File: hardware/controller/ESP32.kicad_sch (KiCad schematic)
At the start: 41 parts, among them J3 Conn_01x05_Pin, Q3 SS8050-G, Q4 SS8050-G, U2 ESP32-S3, Y1 FH4000074Z

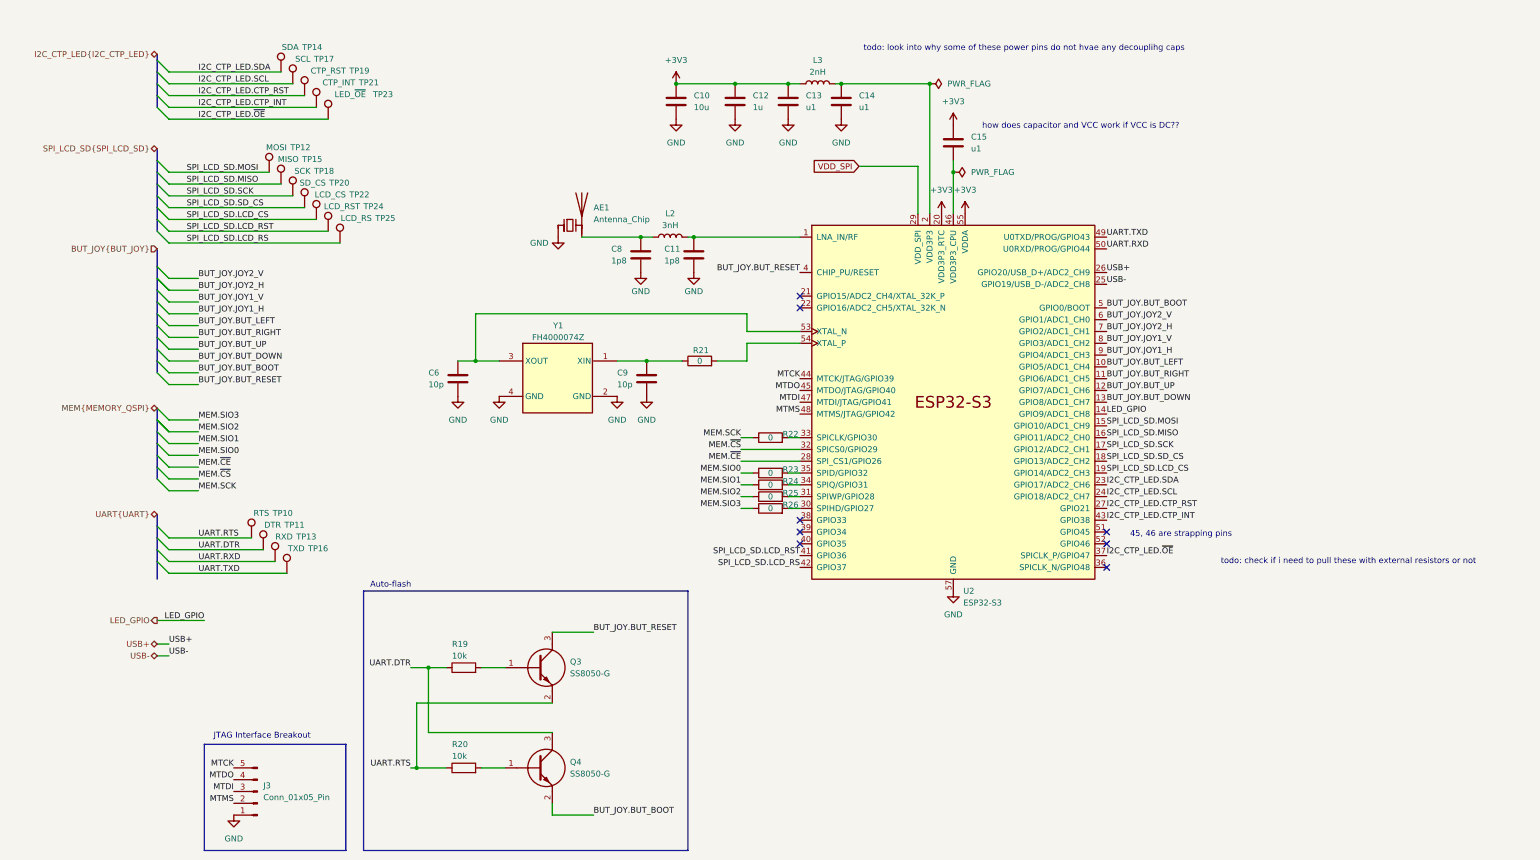
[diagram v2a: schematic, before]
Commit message: ERC good to go. grouped all components on pcb
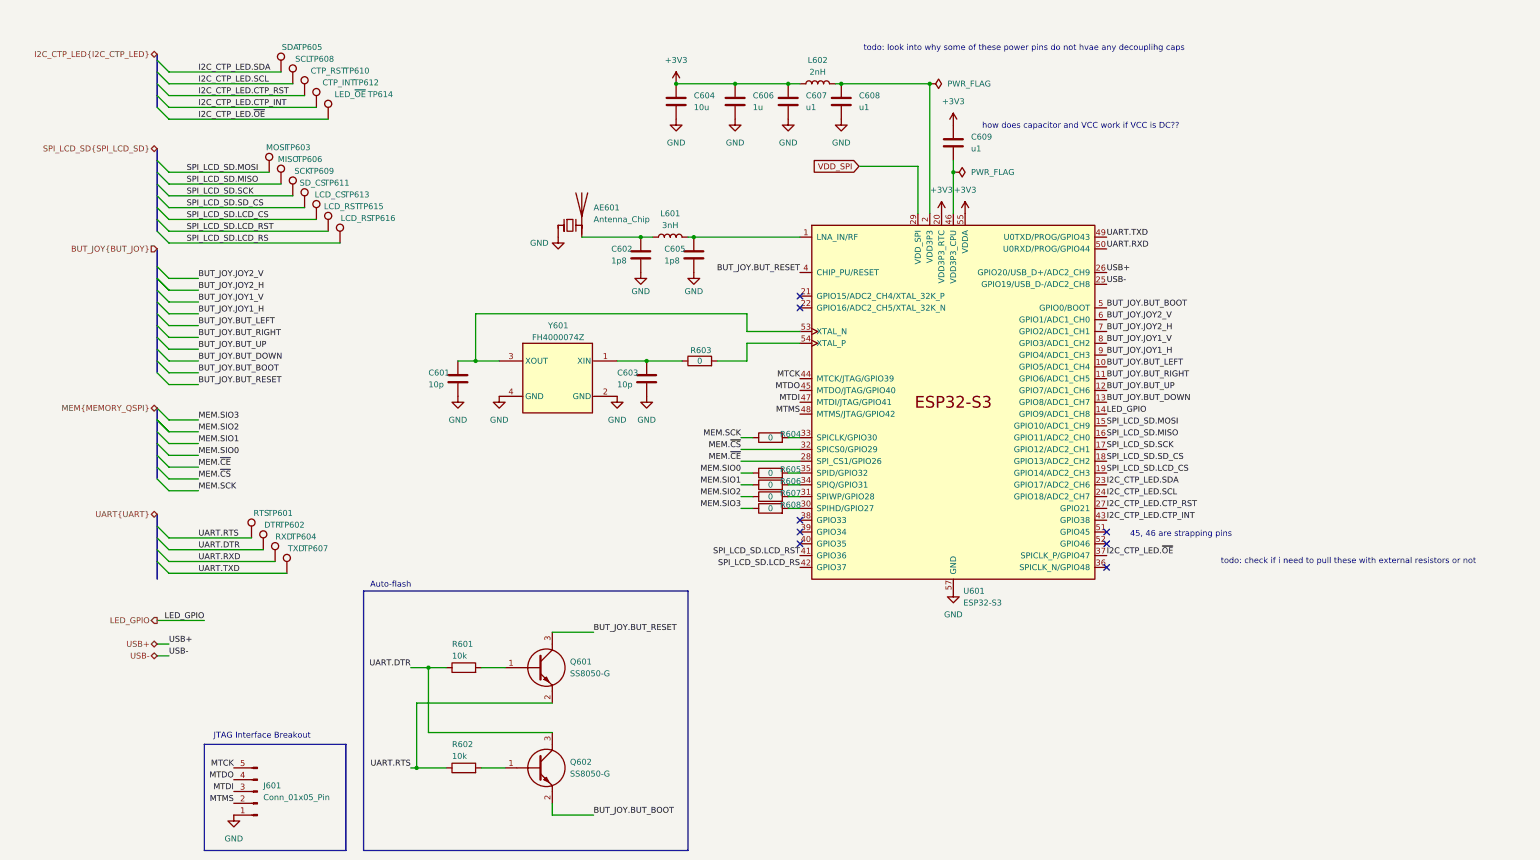
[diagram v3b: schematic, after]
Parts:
- AE601: renamed from AE1; footprint RF_Antenna:Texas_SWRA117D_2.4GHz_Left -> SamacSys_Parts:Texas_SWRA117D_2.4GHz_Left
- C601: renamed from C6; footprint GRT033 -> SamacSys_Parts:CAPC2013X94N; Manufacturer_Name Murata Electronics -> Kyocera AVX; Manufacturer_Part_Number GRT0335C1H100GA02D -> 08053A100JAT2A; Mouser Part Number (none) -> 581-08053A100JAT2A; Mouser Price/Stock (none) -> https://www.mouser.co.uk/ProductDetail/AVX/08053A100JAT2A?q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
- C603: renamed from C9; footprint GRT033 -> SamacSys_Parts:CAPC2013X94N; Manufacturer_Name Murata Electronics -> Kyocera AVX; Manufacturer_Part_Number GRT0335C1H100GA02D -> 08053A100JAT2A; Mouser Part Number (none) -> 581-08053A100JAT2A; Mouser Price/Stock (none) -> https://www.mouser.co.uk/ProductDetail/AVX/08053A100JAT2A?q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
- C604: renamed from C10; footprint CAPC1608X80N -> SamacSys_Parts:CAPC1608X80N
- C606: renamed from C12; footprint CAPC2012X135N -> SamacSys_Parts:CAPC2012X135N
- C607: renamed from C13; footprint MAJx16 -> SamacSys_Parts:MAJx16
- C608: renamed from C14; footprint MAJx16 -> SamacSys_Parts:MAJx16
- C609: renamed from C15; footprint MAJx16 -> SamacSys_Parts:MAJx16
- J601: renamed from J3; footprint Connector_PinHeader_2.54mm:PinHeader_1x04_P2.54mm_Vertical -> Connector_PinHeader_2.54mm:PinHeader_1x05_P2.54mm_Vertical
- L601: renamed from L2; footprint (none) -> SamacSys_Parts:INDC1006X65N; Height (none) -> 0.65; Manufacturer_Name (none) -> ABRACON; Manufacturer_Part_Number (none) -> AIMC-0402HQ-3N0B-T
- L602: renamed from L3; footprint (none) -> SamacSys_Parts:WE-KI_0603A30; Manufacturer_Name (none) -> Wurth Elektronik; Manufacturer_Part_Number (none) -> 744761020A; Mouser Part Number (none) -> 710-744761020A; Mouser Price/Stock (none) -> https://www.mouser.co.uk/ProductDetail/Wurth-Elektronik/744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
- Q601: renamed from Q3; footprint SOT95P240X115-3N -> SamacSys_Parts:SOT95P240X115-3N
- Q602: renamed from Q4; footprint SOT95P240X115-3N -> SamacSys_Parts:SOT95P240X115-3N
- R601: renamed from R19; footprint RESC2012X60N -> SamacSys_Parts:RESC2012X60N
- R602: renamed from R20; footprint RESC2012X60N -> SamacSys_Parts:RESC2012X60N
- R603: renamed from R21; footprint RESC1608X50N -> SamacSys_Parts:RESC1608X50N
- R604: renamed from R22; footprint RESC1608X50N -> SamacSys_Parts:RESC1608X50N
- R605: renamed from R23; footprint RESC1608X50N -> SamacSys_Parts:RESC1608X50N
- R606: renamed from R24; footprint RESC1608X50N -> SamacSys_Parts:RESC1608X50N
- R607: renamed from R25; footprint RESC1608X50N -> SamacSys_Parts:RESC1608X50N
- R608: renamed from R26; footprint RESC1608X50N -> SamacSys_Parts:RESC1608X50N
- Y601: renamed from Y1; footprint FH4000074Z -> SamacSys_Parts:FH4000074Z
- renumbered C8 to C602, C11 to C605, TP10 to TP601, TP11 to TP602, TP12 to TP603, TP13 to TP604, TP14 to TP605, TP15 to TP606, TP16 to TP607, TP17 to TP608, TP18 to TP609, TP19 to TP610, TP20 to TP611, TP21 to TP612, TP22 to TP613, TP23 to TP614, TP24 to TP615, TP25 to TP616, U2 to U601

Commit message: fixed 3d models. rounded edges of pcb
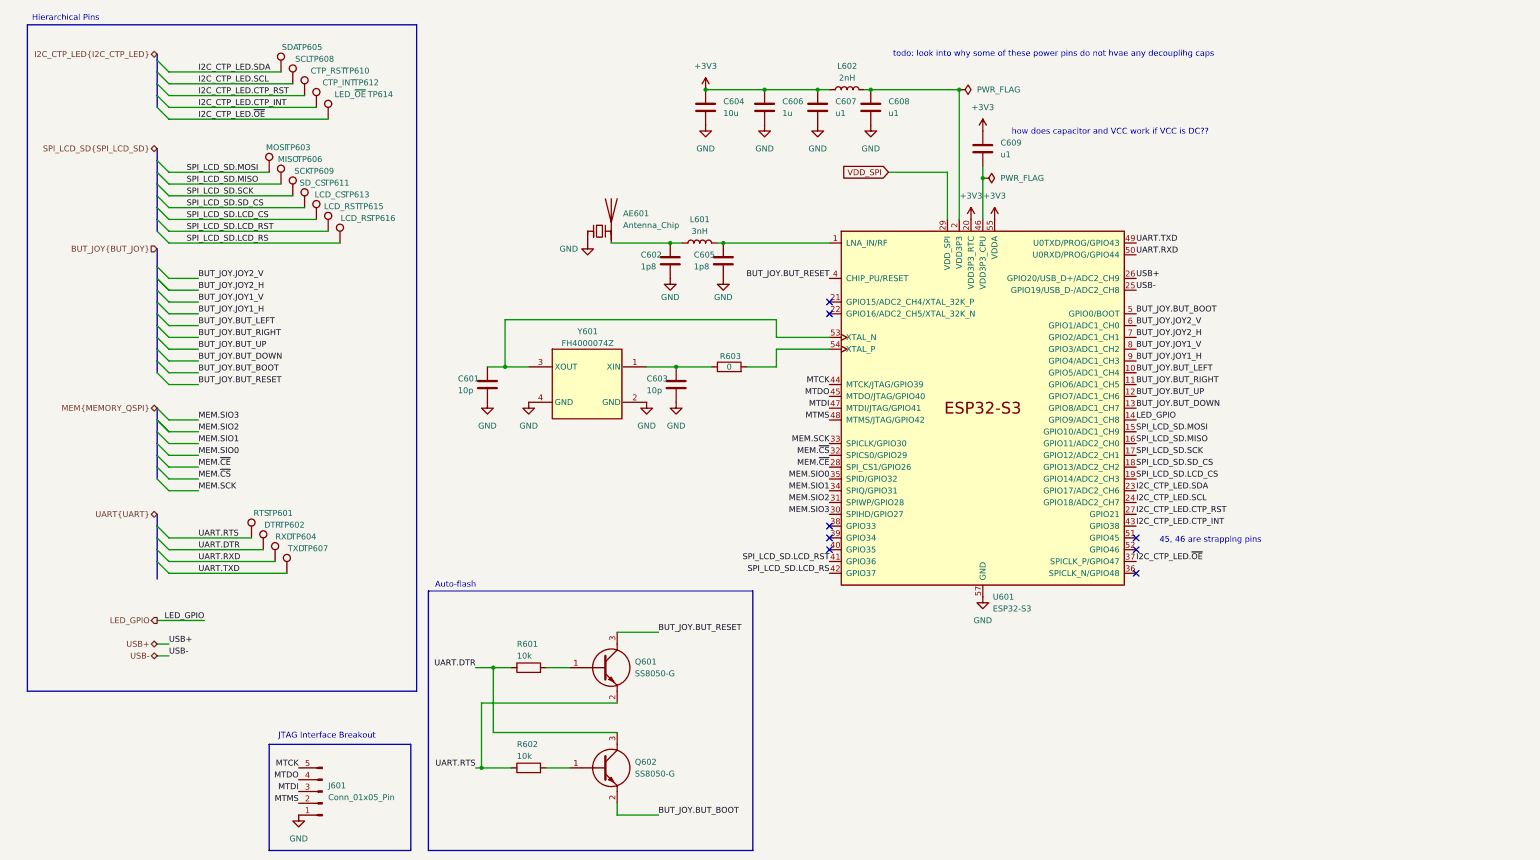
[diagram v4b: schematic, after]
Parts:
- removed R604, R605, R606, R607, R608: 0, SamacSys_Parts:RESC1608X50N, symbol Device:R
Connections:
- net MEM.SCK: now also U601.33 (SPICLK/GPIO30)
- net MEM.SIO0: now also U601.35 (SPID/GPIO32)
- net MEM.SIO1: now also U601.34 (SPIQ/GPIO31)
- net MEM.SIO2: now also U601.31 (SPIWP/GPIO28)
- net MEM.SIO3: now also U601.30 (SPIHD/GPIO27)
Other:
- note added: "Hierarchical Pins"
- note removed: "todo: check if i need to pull these with external resistors or not"
- moved on the sheet: AE601, C601, C602, C603, C604, C605, C606, C607, C608, C609, J601, L601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

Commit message: a
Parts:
- R601, R602: footprint SamacSys_Parts:RESC2012X60N -> RESC2012X60N
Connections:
- net GND: now also AE601.2 (PCB_Trace); no longer AE601.1 (FEED)
- net at C602.1, L601.1: now also AE601.1 (FEED); no longer AE601.2 (PCB_Trace)
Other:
- moved on the sheet: AE601
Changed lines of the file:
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@@
 			)
 		)
-		(property "Footprint" "SamacSys_Parts:RESC2012X60N"
+		(property "Footprint" "RESC2012X60N"
 			(at 219.38 140.97 0)
 			(effects
@@
 			)
 		)
-		(property "Datasheet" "~"
+		(property "Datasheet" "https://componentsearchengine.com/Datasheets/2/ASC0805-10KFT5.pdf"
 			(at 319.38 140.97 0)
 			(effects
@@
 			)
 		)
-		(property "Description" "Resistor"
+		(property "Description" "WELWYN - ASC0805-10KFT5 - RESISTOR, ANTI SULPHUR, 10K, 0.125W, 1%"
 			(at 123.19 154.94 0)
 			(effects
@@
 			)
 		)
-		(property "Footprint" "SamacSys_Parts:RESC2012X60N"
+		(property "Footprint" "RESC2012X60N"
 			(at 219.38 162.56 0)
 			(effects
@@
 			)
 		)
-		(property "Datasheet" "~"
+		(property "Datasheet" "https://componentsearchengine.com/Datasheets/2/ASC0805-10KFT5.pdf"
 			(at 319.38 162.56 0)
 			(effects
@@
 			)
 		)
-		(property "Description" "Resistor"
+		(property "Description" "WELWYN - ASC0805-10KFT5 - RESISTOR, ANTI SULPHUR, 10K, 0.125W, 1%"
 			(at 123.19 176.53 0)
 			(effects
@@
 		(lib_id "Device:Antenna_Chip")
 		(at 138.43 60.96 0)
-		(unit 1)
-		(exclude_from_sim no)
-		(in_bom yes)
-		(on_board yes)
-		(dnp no)
-		(fields_autoplaced yes)
+		(mirror y)
+		(unit 1)
+		(exclude_from_sim no)
+		(in_bom yes)
+		(on_board yes)
+		(dnp no)
 		(property "Reference" "AE601"
-			(at 143.51 57.1499 0)
+			(at 133.35 57.1499 0)
 			(effects
 				(font
@@
 		)
 		(property "Value" "Antenna_Chip"
-			(at 143.51 59.6899 0)
+			(at 133.35 59.6899 0)
 			(effects
 				(font
@@
 		)
 		(property "Footprint" "SamacSys_Parts:Texas_SWRA117D_2.4GHz_Left"
-			(at 135.89 56.515 0)
+			(at 140.97 56.515 0)
 			(effects
 				(font
@@
 		)
 		(property "Datasheet" "~"
-			(at 135.89 56.515 0)
-			(effects
-				(font
+			(at 140.97 56.515 0)
+			(effects
+				(font

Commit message: kicad why crash
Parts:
- Q601, Q602, R601, R602: now not fitted; now left out of the parts list
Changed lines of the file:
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@@
 		(unit 1)
 		(exclude_from_sim no)
-		(in_bom yes)
-		(on_board yes)
-		(dnp no)
+		(in_bom no)
+		(on_board no)
+		(dnp yes)
 		(property "Reference" "R601"
 			(at 120.65 149.86 90)
@@
 		(unit 1)
 		(exclude_from_sim no)
-		(in_bom yes)
-		(on_board yes)
-		(dnp no)
+		(in_bom no)
+		(on_board no)
+		(dnp yes)
 		(fields_autoplaced yes)
 		(property "Reference" "Q601"
@@
 		(unit 1)
 		(exclude_from_sim no)
-		(in_bom yes)
-		(on_board yes)
-		(dnp no)
+		(in_bom no)
+		(on_board no)
+		(dnp yes)
 		(property "Reference" "R602"
 			(at 120.65 171.45 90)
@@
 		(unit 1)
 		(exclude_from_sim no)
-		(in_bom yes)
-		(on_board yes)
-		(dnp no)
+		(in_bom no)
+		(on_board no)
+		(dnp yes)
 		(fields_autoplaced yes)
 		(property "Reference" "Q602"

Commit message: save before nuke
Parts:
- removed R603: 0, SamacSys_Parts:RESC1608X50N, symbol Device:R
- R114: renamed from R601; footprint RESC2012X60N -> SamacSys_Parts:RESC2012X60N
- R115: renamed from R602; footprint RESC2012X60N -> SamacSys_Parts:RESC2012X60N
- renumbered AE601 to AE101, C601 to C108, C602 to C109, C603 to C110, C604 to C111, C605 to C112, C606 to C113, C607 to C114, C608 to C115, C609 to C116, J601 to J103, L601 to L102, L602 to L103, Q601 to Q101, Q602 to Q102, TP601 to TP110, TP602 to TP111, TP603 to TP112, TP604 to TP113, TP605 to TP114, TP606 to TP115, TP607 to TP116, TP608 to TP117, TP609 to TP118, TP610 to TP119, TP611 to TP120, TP612 to TP121, TP613 to TP122, TP614 to TP123, TP615 to TP124, TP616 to TP125, U601 to U102, Y601 to Y101
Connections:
- net BUT_JOY.BUT_DOWN: now also U102.10 (GPIO5/ADC1_CH4); no longer U102.13 (GPIO8/ADC1_CH7)
- net BUT_JOY.BUT_LEFT: now also U102.11 (GPIO6/ADC1_CH5); no longer U102.10 (GPIO5/ADC1_CH4)
- net BUT_JOY.BUT_RIGHT: now also U102.13 (GPIO8/ADC1_CH7); no longer U102.11 (GPIO6/ADC1_CH5)
- net at C110.1, Y101.1 (XIN): now also U102.54 (XTAL_P)

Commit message: done but need to add stitching vias
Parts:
- TP1: renamed from TP110; footprint TestPoint:TestPoint_Pad_1.0x1.0mm -> SamacSys_Parts:TestPoint_Pad_1.0x1.0mm; now not fitted
- TP10: renamed from TP119; footprint TestPoint:TestPoint_Pad_1.0x1.0mm -> 5000; Arrow Part Number (none) -> 5001; Arrow Price/Stock (none) -> https://www.arrow.com/en/products/5001/keystone-electronics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; Manufacturer_Name (none) -> Keystone Electronics; Manufacturer_Part_Number (none) -> 5001; Mouser Part Number (none) -> 534-5001; Mouser Price/Stock (none) -> https://www.mouser.co.uk/ProductDetail/Keystone-Electronics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
- TP11: renamed from TP120; footprint TestPoint:TestPoint_Pad_1.0x1.0mm -> 5000; Arrow Part Number (none) -> 5001; Arrow Price/Stock (none) -> https://www.arrow.com/en/products/5001/keystone-electronics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; Manufacturer_Name (none) -> Keystone Electronics; Manufacturer_Part_Number (none) -> 5001; Mouser Part Number (none) -> 534-5001; Mouser Price/Stock (none) -> https://www.mouser.co.uk/ProductDetail/Keystone-Electronics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
- TP12: renamed from TP121; footprint TestPoint:TestPoint_Pad_1.0x1.0mm -> 5000; Arrow Part Number (none) -> 5001; Arrow Price/Stock (none) -> https://www.arrow.com/en/products/5001/keystone-electronics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; Manufacturer_Name (none) -> Keystone Electronics; Manufacturer_Part_Number (none) -> 5001; Mouser Part Number (none) -> 534-5001; Mouser Price/Stock (none) -> https://www.mouser.co.uk/ProductDetail/Keystone-Electronics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
- TP13: renamed from TP122; footprint TestPoint:TestPoint_Pad_1.0x1.0mm -> 5000; Arrow Part Number (none) -> 5001; Arrow Price/Stock (none) -> https://www.arrow.com/en/products/5001/keystone-electronics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; Manufacturer_Name (none) -> Keystone Electronics; Manufacturer_Part_Number (none) -> 5001; Mouser Part Number (none) -> 534-5001; Mouser Price/Stock (none) -> https://www.mouser.co.uk/ProductDetail/Keystone-Electronics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
- TP14: renamed from TP123; footprint TestPoint:TestPoint_Pad_1.0x1.0mm -> 5000; Arrow Part Number (none) -> 5001; Arrow Price/Stock (none) -> https://www.arrow.com/en/products/5001/keystone-electronics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; Manufacturer_Name (none) -> Keystone Electronics; Manufacturer_Part_Number (none) -> 5001; Mouser Part Number (none) -> 534-5001; Mouser Price/Stock (none) -> https://www.mouser.co.uk/ProductDetail/Keystone-Electronics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
- TP15: renamed from TP124; footprint TestPoint:TestPoint_Pad_1.0x1.0mm -> 5000; Arrow Part Number (none) -> 5001; Arrow Price/Stock (none) -> https://www.arrow.com/en/products/5001/keystone-electronics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; Manufacturer_Name (none) -> Keystone Electronics; Manufacturer_Part_Number (none) -> 5001; Mouser Part Number (none) -> 534-5001; Mouser Price/Stock (none) -> https://www.mouser.co.uk/ProductDetail/Keystone-Electronics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
- TP16: renamed from TP125; footprint TestPoint:TestPoint_Pad_1.0x1.0mm -> 5000; Arrow Part Number (none) -> 5001; Arrow Price/Stock (none) -> https://www.arrow.com/en/products/5001/keystone-electronics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; Manufacturer_Name (none) -> Keystone Electronics; Manufacturer_Part_Number (none) -> 5001; Mouser Part Number (none) -> 534-5001; Mouser Price/Stock (none) -> https://www.mouser.co.uk/ProductDetail/Keystone-Electronics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
- TP2: renamed from TP111; footprint TestPoint:TestPoint_Pad_1.0x1.0mm -> SamacSys_Parts:TestPoint_Pad_1.0x1.0mm; now not fitted
- TP3: renamed from TP112; footprint TestPoint:TestPoint_Pad_1.0x1.0mm -> 5000; Arrow Part Number (none) -> 5001; Arrow Price/Stock (none) -> https://www.arrow.com/en/products/5001/keystone-electronics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; Manufacturer_Name (none) -> Keystone Electronics; Manufacturer_Part_Number (none) -> 5001; Mouser Part Number (none) -> 534-5001; Mouser Price/Stock (none) -> https://www.mouser.co.uk/ProductDetail/Keystone-Electronics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
- TP4: renamed from TP113; footprint TestPoint:TestPoint_Pad_1.0x1.0mm -> SamacSys_Parts:TestPoint_Pad_1.0x1.0mm; now not fitted
- TP5: renamed from TP114; footprint TestPoint:TestPoint_Pad_1.0x1.0mm -> 5000; Arrow Part Number (none) -> 5001; Arrow Price/Stock (none) -> https://www.arrow.com/en/products/5001/keystone-electronics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; Manufacturer_Name (none) -> Keystone Electronics; Manufacturer_Part_Number (none) -> 5001; Mouser Part Number (none) -> 534-5001; Mouser Price/Stock (none) -> https://www.mouser.co.uk/ProductDetail/Keystone-Electronics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
- TP6: renamed from TP115; footprint TestPoint:TestPoint_Pad_1.0x1.0mm -> 5000; Arrow Part Number (none) -> 5001; Arrow Price/Stock (none) -> https://www.arrow.com/en/products/5001/keystone-electronics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; Manufacturer_Name (none) -> Keystone Electronics; Manufacturer_Part_Number (none) -> 5001; Mouser Part Number (none) -> 534-5001; Mouser Price/Stock (none) -> https://www.mouser.co.uk/ProductDetail/Keystone-Electronics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
- TP7: renamed from TP116; footprint TestPoint:TestPoint_Pad_1.0x1.0mm -> SamacSys_Parts:TestPoint_Pad_1.0x1.0mm; now not fitted
- TP8: renamed from TP117; footprint TestPoint:TestPoint_Pad_1.0x1.0mm -> 5000; Arrow Part Number (none) -> 5001; Arrow Price/Stock (none) -> https://www.arrow.com/en/products/5001/keystone-electronics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; Manufacturer_Name (none) -> Keystone Electronics; Manufacturer_Part_Number (none) -> 5001; Mouser Part Number (none) -> 534-5001; Mouser Price/Stock (none) -> https://www.mouser.co.uk/ProductDetail/Keystone-Electronics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
- TP9: renamed from TP118; footprint TestPoint:TestPoint_Pad_1.0x1.0mm -> 5000; Arrow Part Number (none) -> 5001; Arrow Price/Stock (none) -> https://www.arrow.com/en/products/5001/keystone-electronics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; Manufacturer_Name (none) -> Keystone Electronics; Manufacturer_Part_Number (none) -> 5001; Mouser Part Number (none) -> 534-5001; Mouser Price/Stock (none) -> https://www.mouser.co.uk/ProductDetail/Keystone-Electronics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
- renumbered AE101 to AE1, C108 to C1, C109 to C2, C110 to C3, C111 to C4, C112 to C5, C113 to C6, C114 to C7, C115 to C8, C116 to C9, J103 to J1, L102 to L1, L103 to L2, Q101 to Q1, Q102 to Q2, R114 to R1, R115 to R2, U102 to U1, Y101 to Y1
